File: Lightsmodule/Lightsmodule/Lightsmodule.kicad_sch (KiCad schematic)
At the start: 20 parts, among them J1 Conn_01x02_Socket, J2 Conn_01x06_Socket, SW1 SW_Push_SPDT, SW2 SW_Push_SPDT, SW3 SW_Push_SPDT, SW6 SW_Push_SPDT, SW7 SW_Push_SPDT, SW8 SW_Push_SPDT, U1 TLC555xD

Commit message: Board Layout and Assignment. Pending Buzzer
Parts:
- removed F1, F2, F3, F4, F5, F6, F7: Fuse, symbol Device:Fuse
- added BZ1: Buzzer, symbol Device:Buzzer
- added D1, D2, D3, D4, D5: LED, Library:LED_D3.0mm, symbol Device:LED
- added H1, H2, H3: MountingHole, MountingHole:MountingHole_4.3mm_M4, symbol Mechanical:MountingHole
- added Q5: Q_NMOS_GSD, Package_TO_SOT_SMD:SOT-23, symbol Transistor_FET:Q_NMOS_GSD
- added R10, R11: 2M, Resistor_SMD:R_0402_1005Metric, symbol Device:R
- added R3, R4: 1.8k, Resistor_SMD:R_0603_1608Metric, symbol Device:R
- added R5, R6, R7, R8, R9: 10k, Resistor_SMD:R_0402_1005Metric, symbol Device:R
- added U2, U3: TLP3553A, Library:SOIC_3553ATP1_F_TOS, symbol Relay_SolidState:TLP222A
- C1, C2: footprint (none) -> Capacitor_SMD:C_0603_1608Metric; MPN (none) -> CL10B474KA8NFNC
- J1: footprint (none) -> Library:CUI_TB002-500-02BE; MPN (none) -> TB002-500-02BE
- J2: footprint (none) -> Library:CUI_TB002-500-06BE; MPN (none) -> TB002-500-06BE
- R1: MPN (none) -> CRCW04022M00FKED
- R2: value 1K -> 1.8k; footprint Resistor_SMD:R_0805_2012Metric -> Resistor_SMD:R_0603_1608Metric; MPN (none) -> ERJ-PA3F1801V
- SW1, SW2, SW6, SW7, SW8: footprint (none) -> Library:100SPxT1B1M2QEH
- SW3: footprint (none) -> Library:100SPxT1B1M2QEH; MPN 100SP1T1B1M2QEH -> 100SP2T1B1M2QEH
- U1: MPN (none) -> TLC555QDRQ1
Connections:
- net RST is gone; now on net +12V: U1.4 (R)
- net +12V: now also J1.1 (Pin_1), BZ1.1 (+), R10.1, U2.4, U3.4; no longer SW1.2 (B), SW2.2 (B)
- net BRIGHT: now also J2.2 (Pin_2), R7.1
- net FOG: now also J2.4 (Pin_4), R6.1
- net GND: now also D1.1 (K), D2.1 (K), D3.1 (K), D4.1 (K), D5.1 (K), Q5.2 (S), R11.2, U2.2, U3.2
- net HEADLIGHT: now also J2.3 (Pin_3), R5.1
- net HORN: now also J2.1 (Pin_1)
- net LEFT_EN: now also SW1.2 (B), R4.1, R8.1; no longer SW1.1 (A)
- net L_OUT: now also J2.5 (Pin_5), U2.3
- net OUT: now also SW1.1 (A), SW2.1 (A), Q5.1 (G), R11.1
- net RIGHT_EN: now also SW2.2 (B), R3.1, R9.1; no longer SW2.1 (A)
- net R_OUT: now also J2.6 (Pin_6), U3.3
- new net: R4.2, U2.1
- new net: D3.2 (A), R7.2
- new net: D1.2 (A), R5.2
- new net: D5.2 (A), R9.2
- new net: BZ1.2 (-), Q5.3 (D), R10.2
- new net: D2.2 (A), R6.2
- new net: D4.2 (A), R8.2
- new net: R3.2, U3.1
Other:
- note added: "1.64V forward, ~12V out, 12(-1.64)/1800 = ~6mA ~65mW disipation"
- note added: "Amber"
- note added: "Assumes External Fuse"
- note added: "Assumes Fuse outside"
- note added: "Blue"
- note added: "Can see 12mA here"
- note added: "FOG: ON/ON"
- note added: "Green"
- note added: "Headlight: ON/ON"
- note added: "Horn: ON/MOM"
- note added: "Left: ON/ON"
- note added: "Right: ON/ON"
- note added: "TODO Drive for 1mA on these indicators?"
- note added: "TODO Write these out in silkscreen"
- note added: "TODO test locally. need to confirm that this works on AC/ Externally driven"
- note added: "Tip of LED needs to be at about 8.8->8.9mm"
- note added: "White"
- note removed: "ON/MOM"
- note removed: "ON/ON"
- moved on the sheet: J1

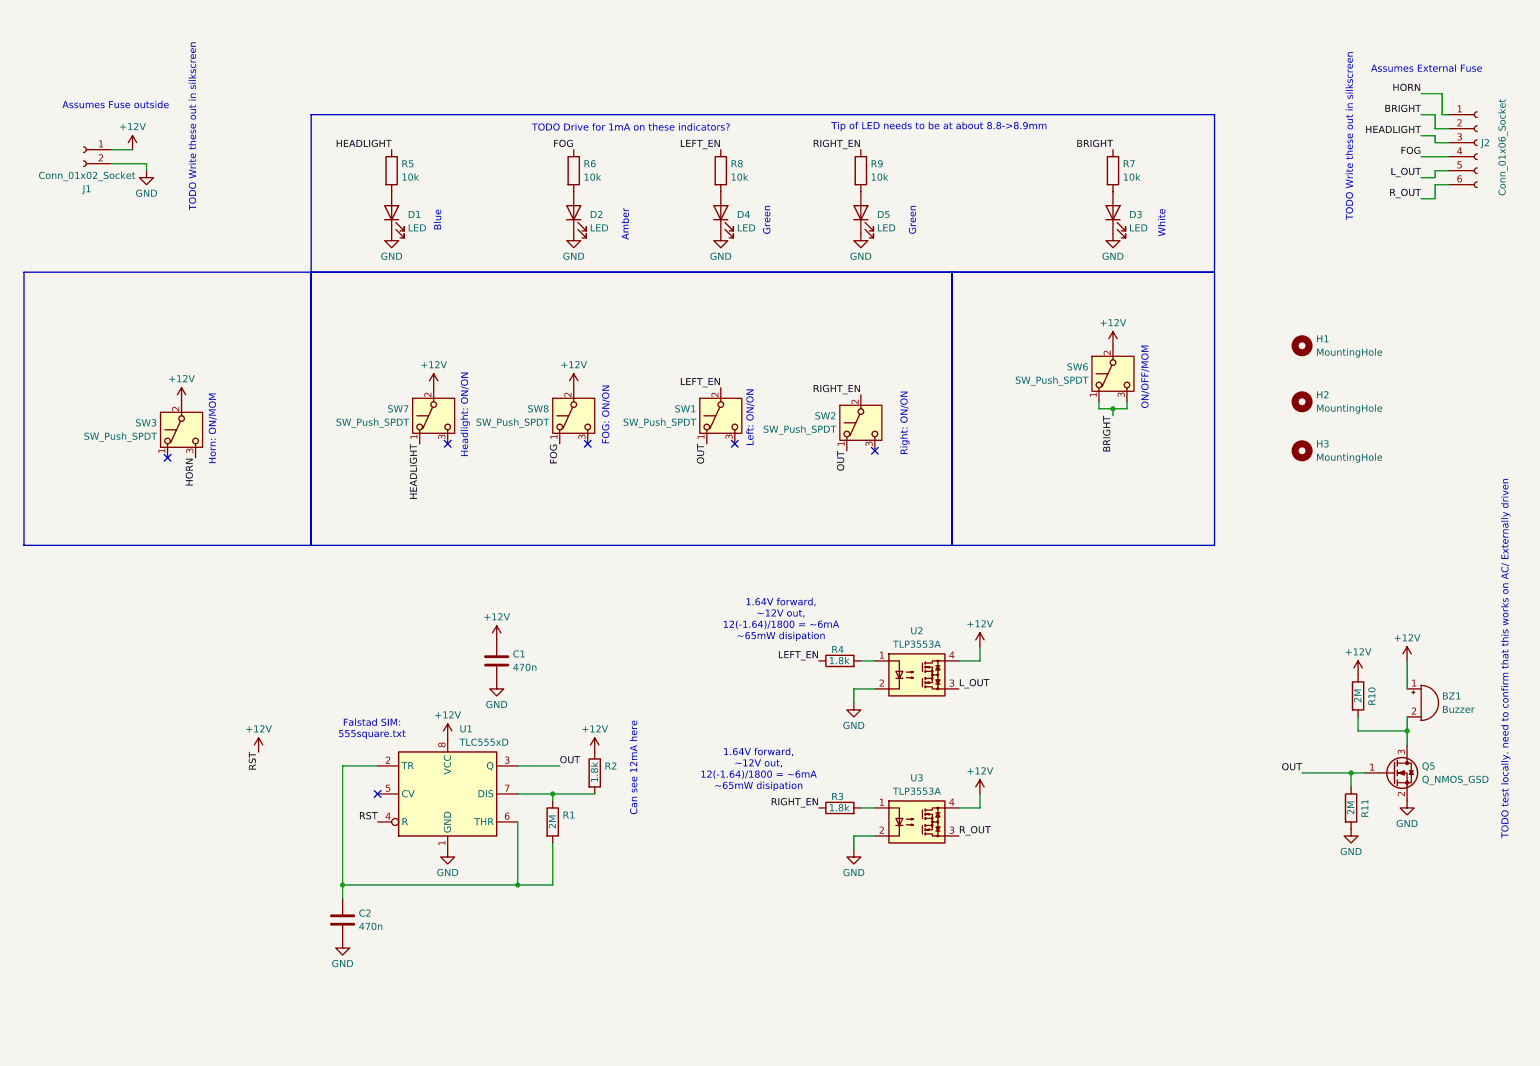
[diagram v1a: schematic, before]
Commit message: In Theory working Timing / Buzzer Circuit
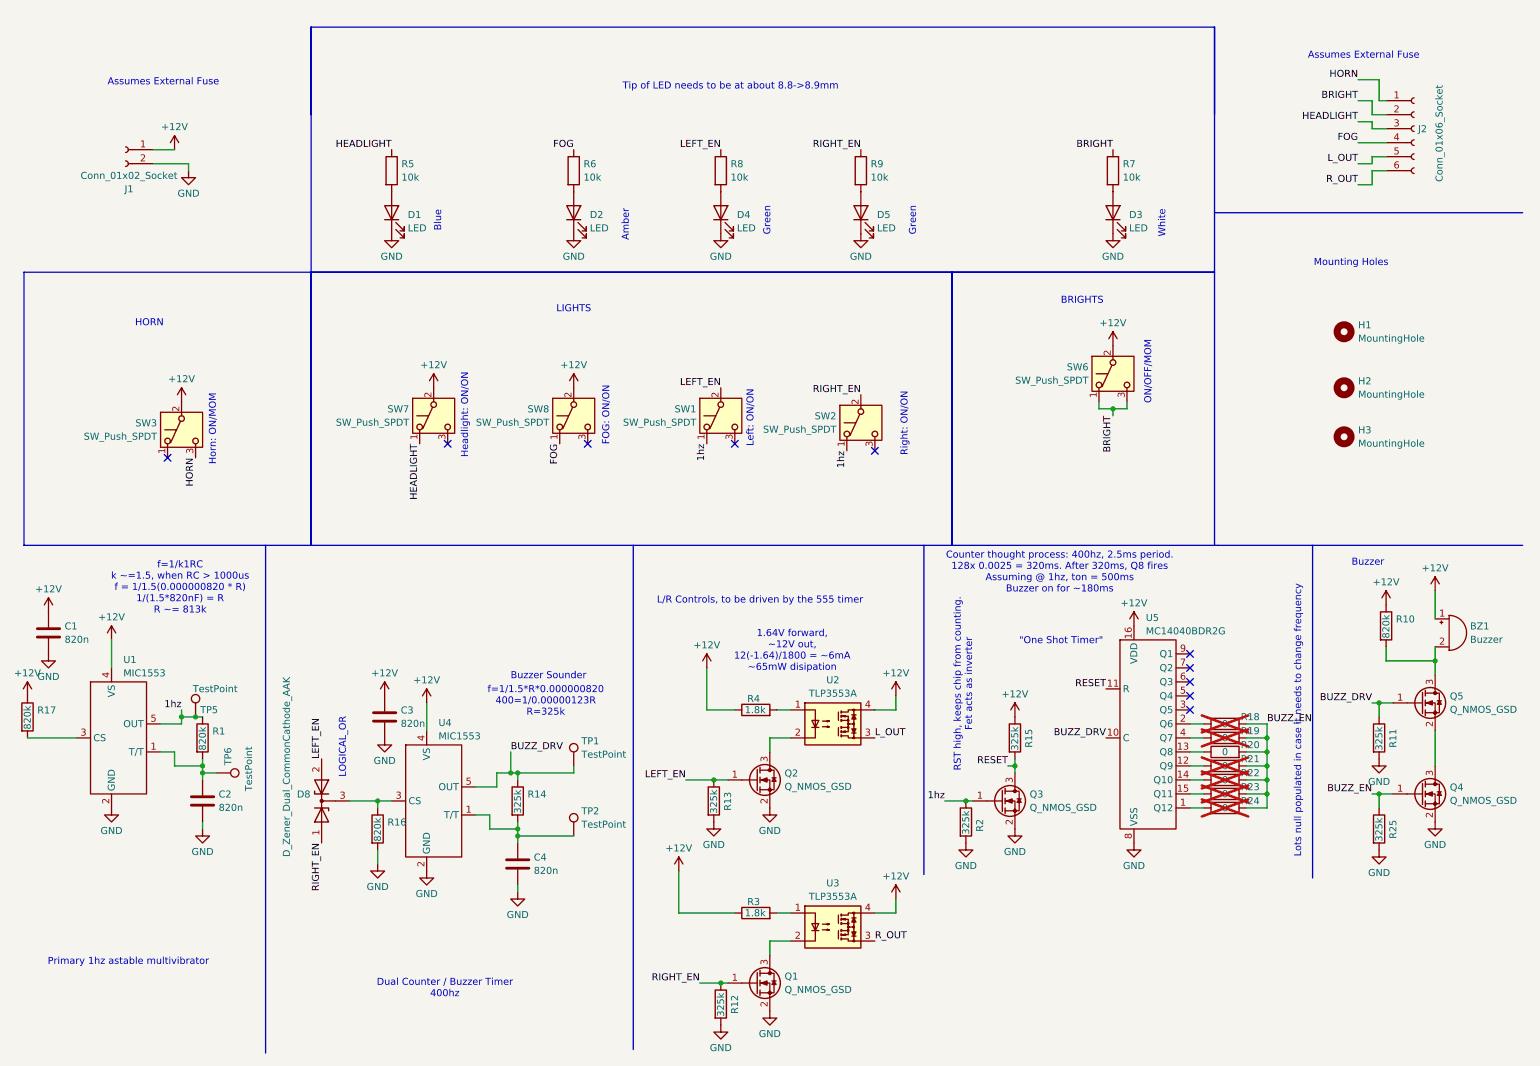
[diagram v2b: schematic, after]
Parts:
- removed U1: TLC555xD, Package_SO:SOIC-8_3.9x4.9mm_P1.27mm, symbol Timer:TLC555xD
- added C3, C4: 820n, Capacitor_SMD:C_0603_1608Metric, symbol Device:C
- added D8: D_Zener_Dual_CommonCathode_AAK, Package_TO_SOT_SMD:SOT-23, symbol Device:D_Zener_Dual_CommonCathode_AAK
- added Q1, Q2, Q3, Q4: Q_NMOS_GSD, Package_TO_SOT_SMD:SOT-23, symbol Transistor_FET:Q_NMOS_GSD
- added R12, R13, R14, R15, R25: 325k, Resistor_SMD:R_0402_1005Metric, symbol Device:R
- added R16, R17: 820k, Resistor_SMD:R_0402_1005Metric, symbol Device:R
- added R18, R19, R20, R21, R22, R23, R24: 0, Resistor_SMD:R_0402_1005Metric, symbol Device:R
- added TP1, TP2, TP5, TP6: TestPoint, TestPoint:TestPoint_Pad_1.0x1.0mm, symbol Connector:TestPoint
- added U1, U4: MIC1553, Package_TO_SOT_SMD:SOT-23-5, symbol New_Library:MIC1553YM5-TR
- added U5: MC14040BDR2G, Package_SO:SOIC-16_3.9x9.9mm_P1.27mm, symbol New_Library:MC14040BDR2G
- BZ1: footprint (none) -> Library:CUI_CEM-1212S
- C1, C2: value 470n -> 820n; MPN CL10B474KA8NFNC -> (none)
- R1, R10: value 2M -> 820k; MPN CRCW04022M00FKED -> (none)
- R11: value 2M -> 325k
- R2: value 1.8k -> 325k; footprint Resistor_SMD:R_0603_1608Metric -> Resistor_SMD:R_0402_1005Metric; MPN ERJ-PA3F1801V -> CRCW04022M00FKED
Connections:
- net +12V: now also R3.1, R4.1, C3.1, R15.1, R17.1, U1.4 (VS), U4.4 (VS), U5.16 (VDD); no longer R2.1
- net GND: now also R2.2, C3.2, C4.2, Q1.2 (S), Q2.2 (S), Q3.2 (S), Q4.2 (S), R12.2, R13.2, R16.2, R25.2, U1.2 (GND), U4.2 (GND), U5.8 (VSS); no longer Q5.2 (S), U2.2, U3.2
- net LEFT_EN: now also D8.2 (A), Q2.1 (G), R13.1; no longer R4.1
- net RIGHT_EN: now also D8.1 (A), Q1.1 (G), R12.1; no longer R3.1
- net at C2.1, R1.2: now also TP6.1, U1.1 (T/T)
- net 1hz: now reaches R1.1
- net 1hz: now also R2.1, SW1.1 (A), SW2.1 (A), Q3.1 (G), TP5.1, U1.5 (OUT); no longer R2.2
- net OUT renamed BUZZ_DRV
- net BUZZ_DRV: now also R14.1, TP1.1, U4.5 (OUT), U5.10 (C); no longer SW1.1 (A), SW2.1 (A)
- new net: R21.1, U5.12 (Q9)
- new net: R17.2, U1.3 (CS)
- new net: Q2.3 (D), U2.2
- new net: R22.1, U5.14 (Q10)
- new net: R24.1, U5.1 (Q12)
- new net: C4.1, R14.2, TP2.1, U4.1 (T/T)
- new net: D8.3 (K), R16.1, U4.3 (CS)
- new net: Q4.3 (D), Q5.2 (S)
- new net: Q1.3 (D), U3.2
- new net: R20.1, U5.13 (Q8)
- new net: R23.1, U5.15 (Q11)
- new net: R18.1, U5.2 (Q6)
- new net: R19.1, U5.4 (Q7)
- new net BUZZ_EN: Q4.1 (G), R18.2, R19.2, R20.2, R21.2, R22.2, R23.2, R24.2, R25.1
- new net RESET: Q3.3 (D), R15.2, U5.11 (R)
- no-connect marks 6 -> 10
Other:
- note added: ""One Shot Timer""
- note added: "BRIGHTS"
- note added: "Buzzer"
- note added: "Buzzer Sounder"
- note added: "Counter thought process: 400hz, 2.5ms period. 128x 0.0025 = 320ms. After 320ms, Q8 fires Assuming @ 1hz, ton = 500ms Buzzer on for ~180ms"
- note added: "Dual Counter / Buzzer Timer 400hz"
- note added: "HORN"
- note added: "L/R Controls, to be driven by the 555 timer"
- note added: "LIGHTS"
- note added: "LOGICAL_OR"
- note added: "Lots null populated in case it needs to change frequency"
- note added: "Mounting Holes"
- note added: "Primary 1hz astable multivibrator"
- note added: "RST high, keeps chip from counting. Fet acts as inverter"
- note added: "f=1/1.5*R*0.000000820 400=1/0.00000123R R=325k"
- note added: "f=1/k1RC k ~=1.5, when RC > 1000us f = 1/1.5(0.000000820 * R) 1/(1.5*820nF) = R R ~= 813k"
- note removed: "Assumes Fuse outside"
- note removed: "Can see 12mA here"
- note removed: "Falstad SIM: 555square.txt"
- note removed: "TODO Drive for 1mA on these indicators?"
- note removed: "TODO Write these out in silkscreen"
- note removed: "TODO test locally. need to confirm that this works on AC/ Externally driven"
- moved on the sheet: BZ1, H1, H2, H3, J1, J2, Q5, R11, R3, R4, U2, U3

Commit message: New Layout based on more spread out Switches
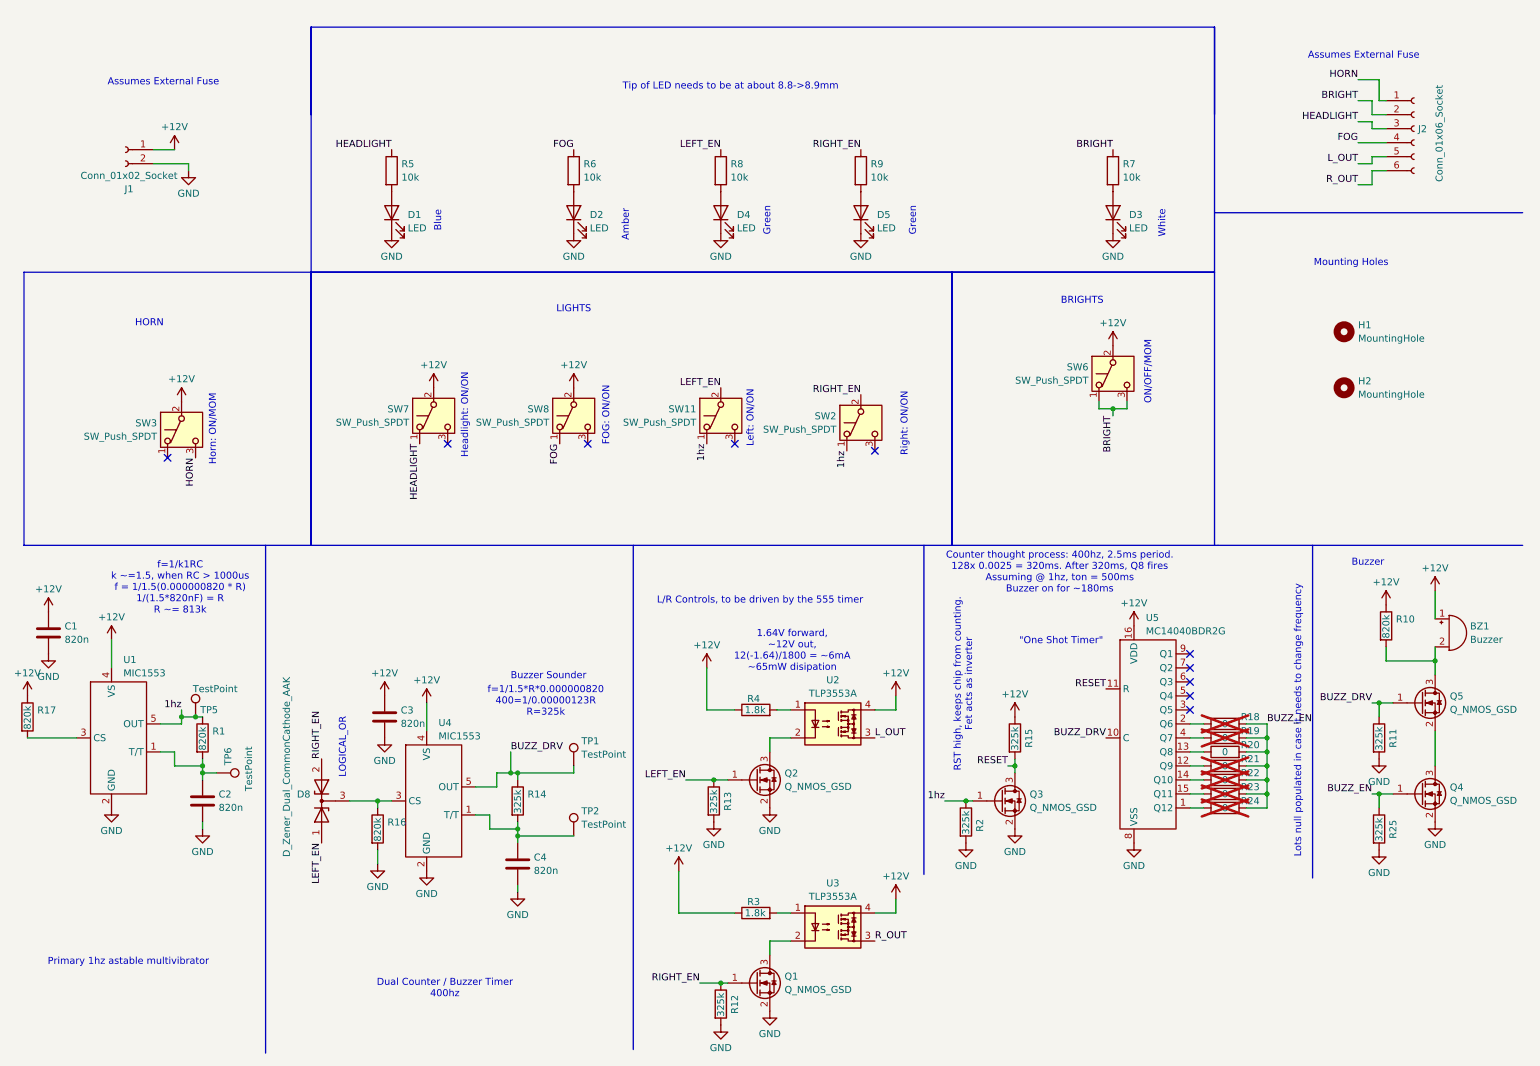
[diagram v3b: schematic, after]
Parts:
- removed H3: MountingHole, MountingHole:MountingHole_4.3mm_M4, symbol Mechanical:MountingHole
- BZ1: footprint Library:CUI_CEM-1212S -> (none)
- renumbered SW1 to SW11
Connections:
- net LEFT_EN: now also D8.1 (A); no longer D8.2 (A)
- net RIGHT_EN: now also D8.2 (A); no longer D8.1 (A)
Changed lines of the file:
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@@
 		)
 	)
+	(label "RIGHT_EN"
+		(at 67.31 144.78 90)
+		(effects
+			(font
+				(size 1.27 1.27)
+			)
+			(justify left bottom)
+		)
+	)
 	(label "HORN"
 		(at 44.45 90.17 270)
@@
 	)
 	(label "LEFT_EN"
-		(at 67.31 144.78 90)
+		(at 67.31 160.02 270)
 		(effects
 			(font
 				(size 1.27 1.27)
 			)
-			(justify left bottom)
+			(justify right bottom)
 		)
 	)
@@
 		)
 	)
-	(label "RIGHT_EN"
-		(at 67.31 160.02 270)
-		(effects
-			(font
-				(size 1.27 1.27)
-			)
-			(justify right bottom)
-		)
-	)
 	(label "LEFT_EN"
 		(at 139.7 77.47 180)
@@
 			)
 		)
-		(property "Footprint" "Library:CUI_CEM-1212S"
+		(property "Footprint" ""
 			(at 271.145 119.38 90)
 			(effects
@@
 	)
 	(symbol
-		(lib_id "Mechanical:MountingHole")
-		(at 252.73 86.36 0)
-		(unit 1)
-		(exclude_from_sim no)
-		(in_bom no)
-		(on_board yes)
-		(dnp no)
-		(fields_autoplaced yes)
-		(property "Reference" "H3"
-			(at 255.27 85.1478 0)
-			(effects
-				(font
-					(size 1.27 1.27)
-				)
-				(justify left)
-			)
-		)
-		(property "Value" "MountingHole"
-			(at 255.27 87.5721 0)
-			(effects
-				(font
-					(size 1.27 1.27)
-				)
-				(justify left)
-			)
-		)
-		(property "Footprint" "MountingHole:MountingHole_4.3mm_M4"
-			(at 252.73 86.36 0)
-			(effects
-				(font
-					(size 1.27 1.27)
-				)
-				(hide yes)
-			)
-		)
-		(property "Datasheet" "~"
-			(at 252.73 86.36 0)
-			(effects
-				(font
-					(size 1.27 1.27)
-				)
-				(hide yes)
-			)
-		)
-		(property "Description" "Mounting Hole without connection"
-			(at 252.73 86.36 0)
-			(effects
-				(font
-					(size 1.27 1.27)
-				)
-				(hide yes)
-			)
-		)
-		(instances
-			(project "Lightsmodule"
-				(path "/15738d50-cc27-46ea-b201-adde7f892d56"
-					(reference "H3")
-					(unit 1)
-				)
-			)
-		)
-	)
-	(symbol
 		(lib_id "Device:C")
 		(at 17.78 121.92 0)
@@
 		(on_board yes)
 		(dnp no)
-		(property "Reference" "SW1"
+		(property "Reference" "SW11"
 			(at 135.255 81.3378 90)
 			(effects
@@
 			(project "Lightsmodule"
 				(path "/15738d50-cc27-46ea-b201-adde7f892d56"
-					(reference "SW1")
+					(reference "SW11")
 					(unit 1)
 				)
